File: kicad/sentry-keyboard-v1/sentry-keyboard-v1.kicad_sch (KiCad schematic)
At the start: 184 parts, among them J1 USB_C_Receptacle_USB2.0, J4 AVR-ISP-6, SW1 Reset, U1 ATmega32U4-AU, U3 PRTR5V0U2X, Y1 16Mhz

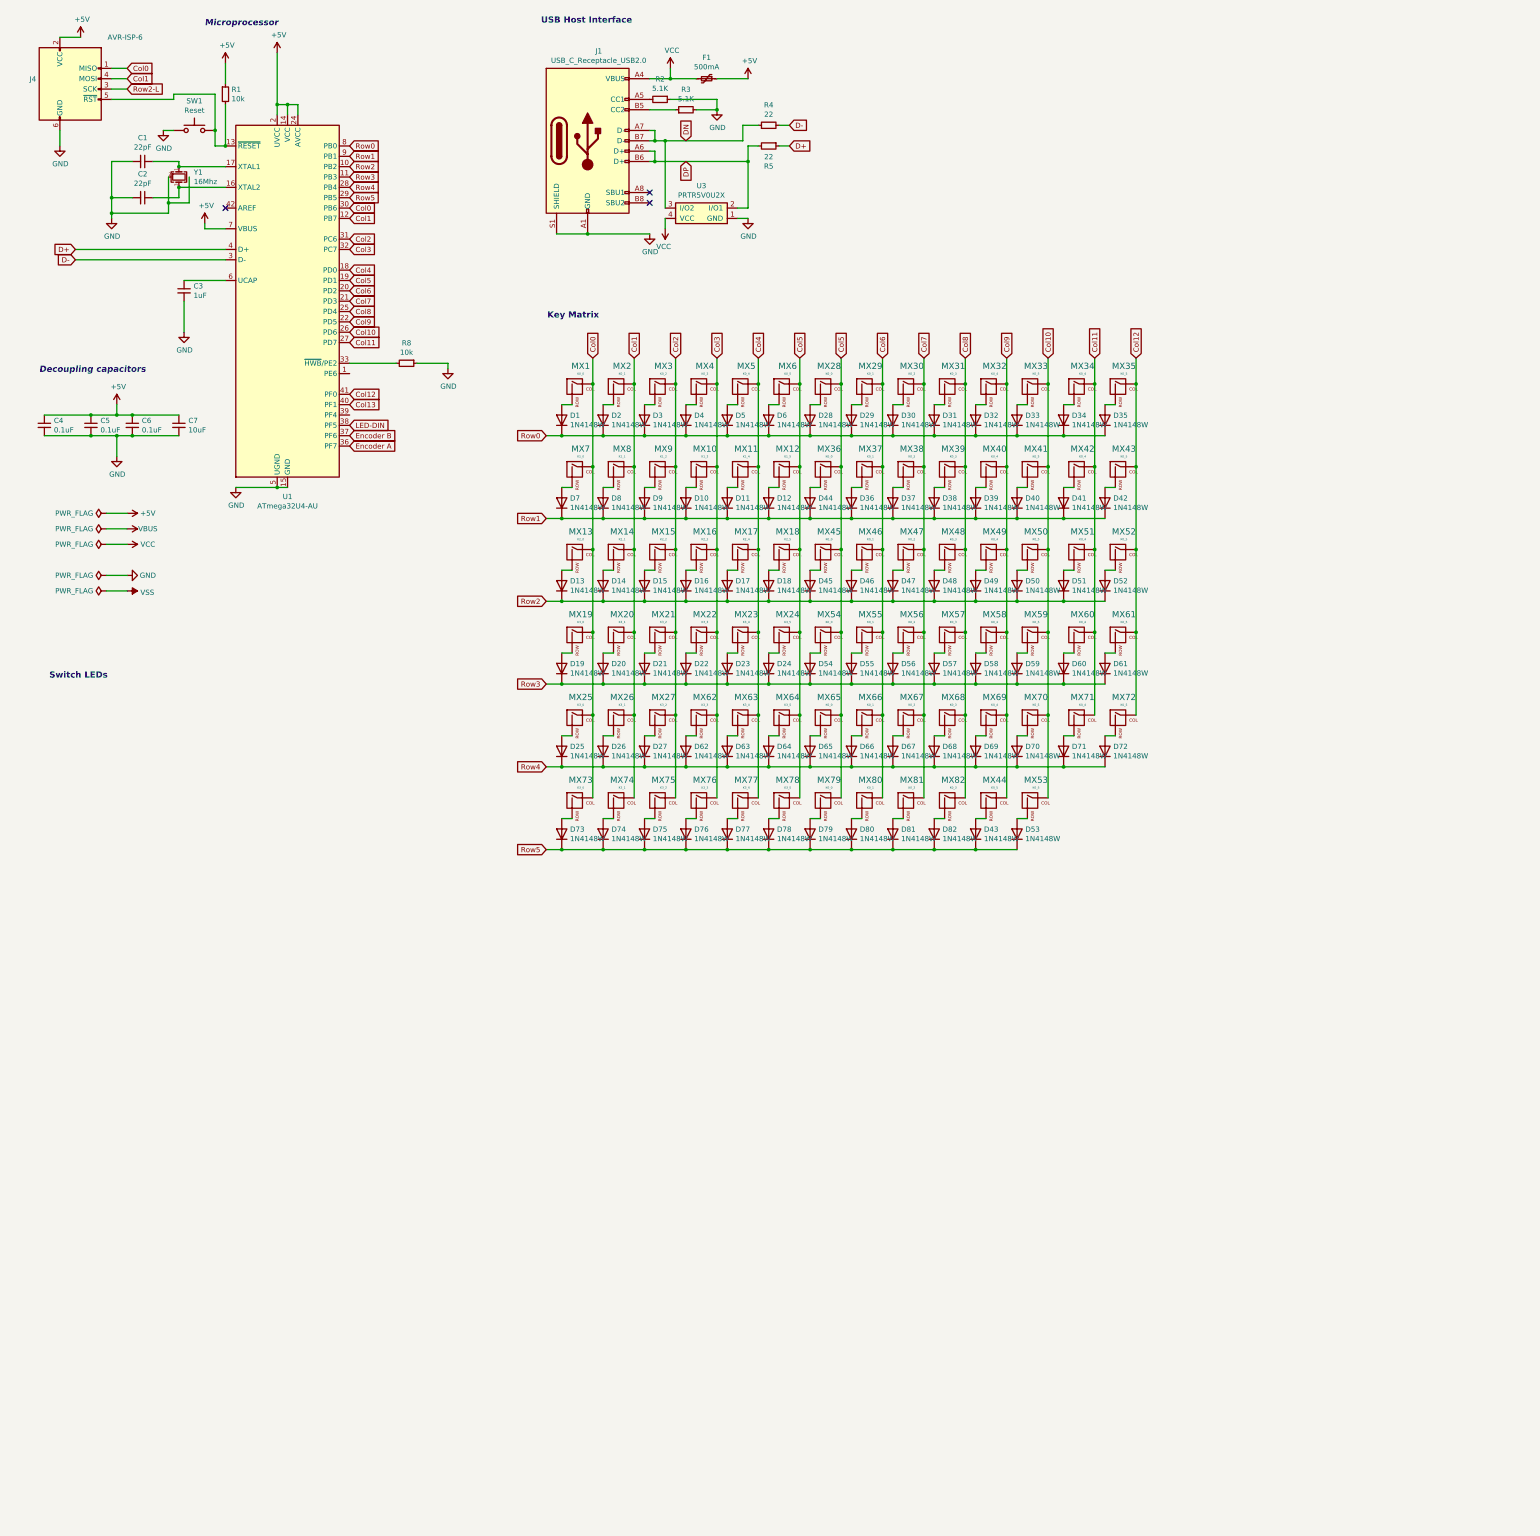
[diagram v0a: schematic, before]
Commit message: Add first draft of LED matrix
Need to figure out if each LED needs a 100uf capacitor, and if the data
line needs a resistor still. The datasheet is really hard to read
because of low quality scan.
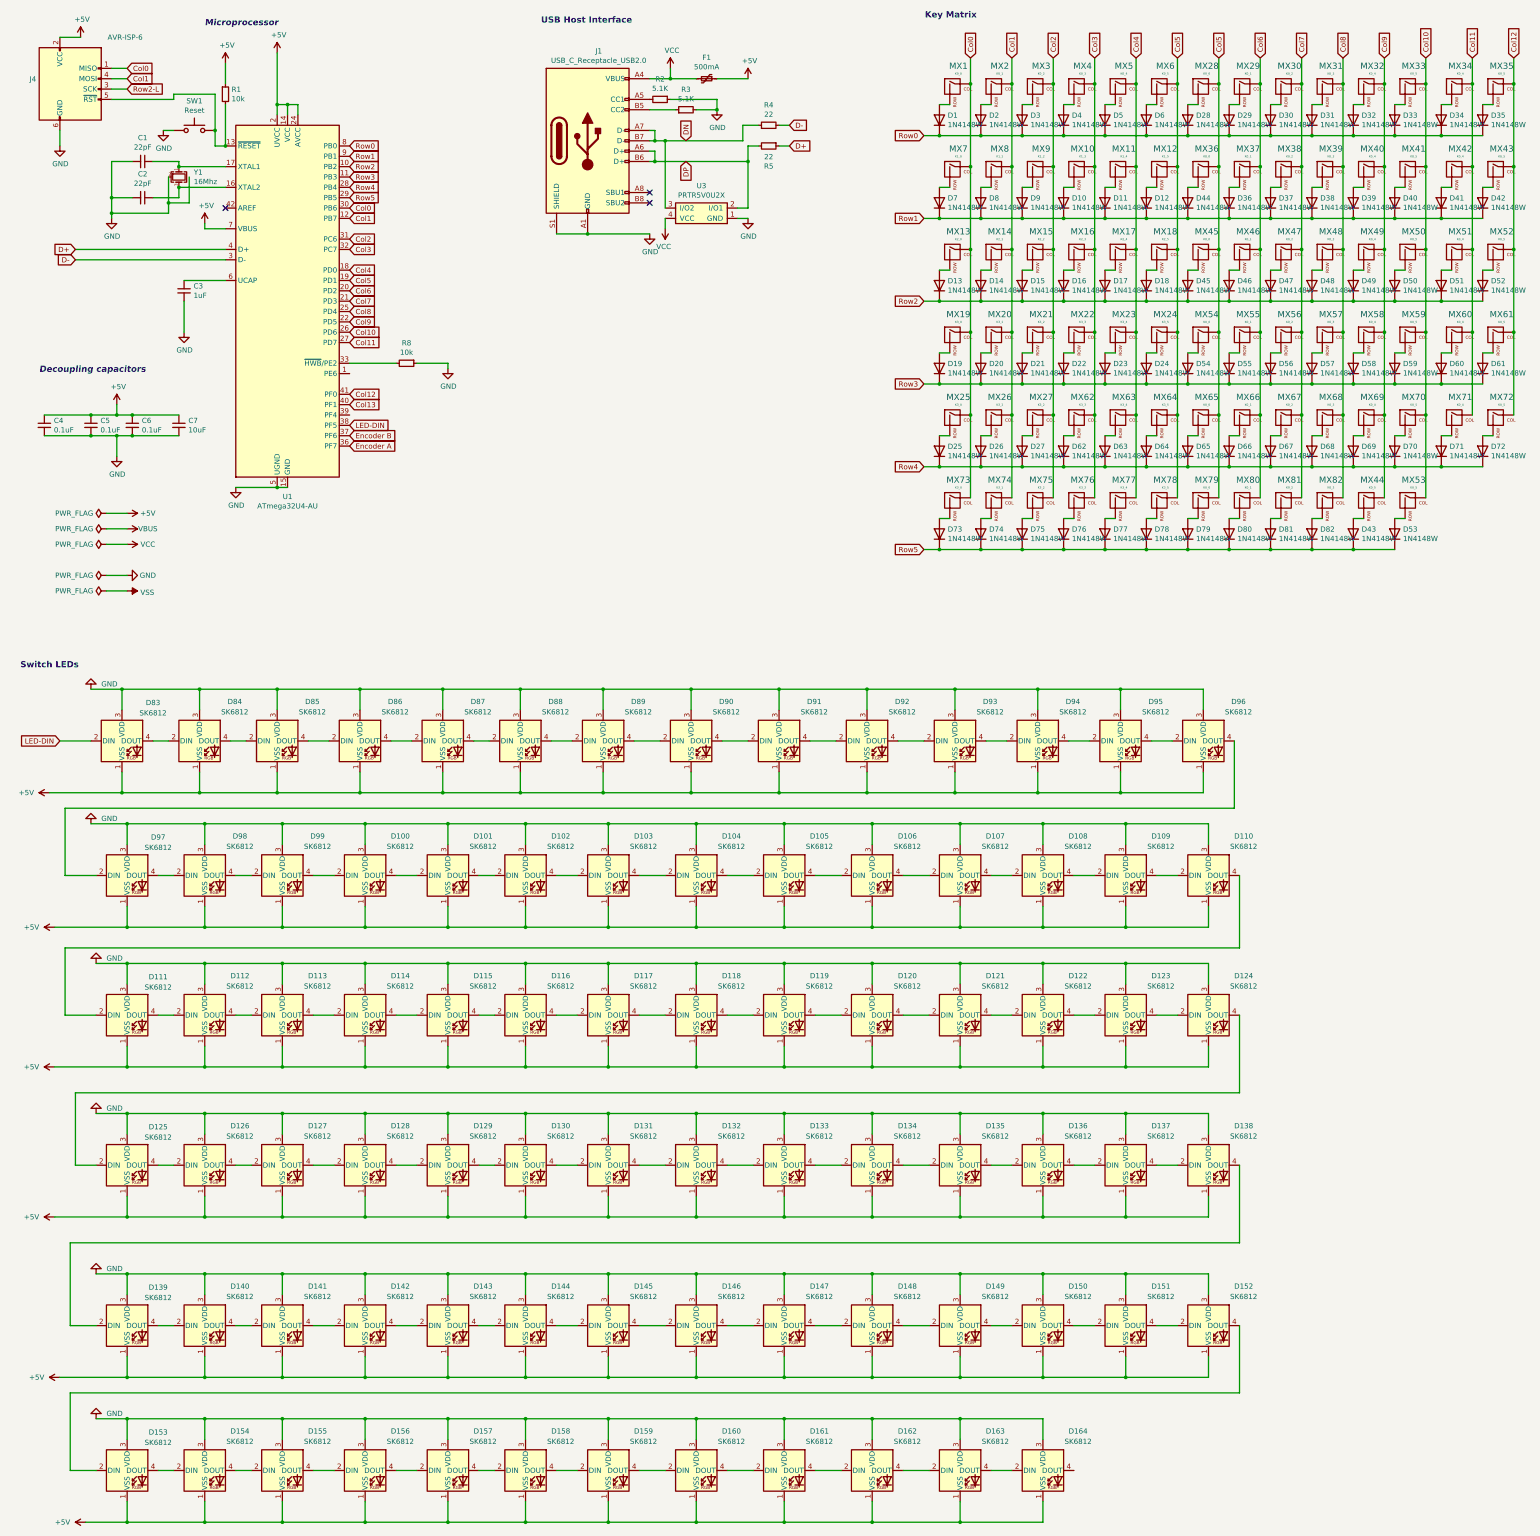
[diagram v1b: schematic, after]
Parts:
- added D100, D101, D102, D103, D104, D105, D106, D107, D108, D109, D110, D111, D112, D113, D114, D115, D116, D117, D118, D119, D120, D121, D122, D123, D124, D125, D126, D127, D128, D129, D130, D131, D132, D133, D134, D135, D136, D137, D138, D139, D140, D141, D142, D143, D144, D145, D146, D147, D148, D149, D150, D151, D152, D153, D154, D155, D156, D157, D158, D159, D160, D161, D162, D163, D164, D83, D84, D85, D86, D87, D88, D89, D90, D91, D92, D93, D94, D95, D96, D97, D98, D99: SK6812, LED_SMD:LED_SK6812_PLCC4_5.0x5.0mm_P3.2mm, symbol LED:SK6812
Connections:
- net +5V: now also D100.1 (VSS), D101.1 (VSS), D102.1 (VSS), D103.1 (VSS), D104.1 (VSS), D105.1 (VSS), D106.1 (VSS), D107.1 (VSS), D108.1 (VSS), D109.1 (VSS), D110.1 (VSS), D111.1 (VSS), D112.1 (VSS), D113.1 (VSS), D114.1 (VSS), D115.1 (VSS), D116.1 (VSS), D117.1 (VSS), D118.1 (VSS), D119.1 (VSS), D120.1 (VSS), D121.1 (VSS), D122.1 (VSS), D123.1 (VSS), D124.1 (VSS), D125.1 (VSS), D126.1 (VSS), D127.1 (VSS), D128.1 (VSS), D129.1 (VSS), D130.1 (VSS), D131.1 (VSS), D132.1 (VSS), D133.1 (VSS), D134.1 (VSS), D135.1 (VSS), D136.1 (VSS), D137.1 (VSS), D138.1 (VSS), D139.1 (VSS), D140.1 (VSS), D141.1 (VSS), D142.1 (VSS), D143.1 (VSS), D144.1 (VSS), D145.1 (VSS), D146.1 (VSS), D147.1 (VSS), D148.1 (VSS), D149.1 (VSS), D150.1 (VSS), D151.1 (VSS), D152.1 (VSS), D153.1 (VSS), D154.1 (VSS), D155.1 (VSS), D156.1 (VSS), D157.1 (VSS), D158.1 (VSS), D159.1 (VSS), D160.1 (VSS), D161.1 (VSS), D162.1 (VSS), D163.1 (VSS), D164.1 (VSS), D83.1 (VSS), D84.1 (VSS), D85.1 (VSS), D86.1 (VSS), D87.1 (VSS), D88.1 (VSS), D89.1 (VSS), D90.1 (VSS), D91.1 (VSS), D92.1 (VSS), D93.1 (VSS), D94.1 (VSS), D95.1 (VSS), D96.1 (VSS), D97.1 (VSS), D98.1 (VSS), D99.1 (VSS)
- net GND: now also D100.3 (VDD), D101.3 (VDD), D102.3 (VDD), D103.3 (VDD), D104.3 (VDD), D105.3 (VDD), D106.3 (VDD), D107.3 (VDD), D108.3 (VDD), D109.3 (VDD), D110.3 (VDD), D111.3 (VDD), D112.3 (VDD), D113.3 (VDD), D114.3 (VDD), D115.3 (VDD), D116.3 (VDD), D117.3 (VDD), D118.3 (VDD), D119.3 (VDD), D120.3 (VDD), D121.3 (VDD), D122.3 (VDD), D123.3 (VDD), D124.3 (VDD), D125.3 (VDD), D126.3 (VDD), D127.3 (VDD), D128.3 (VDD), D129.3 (VDD), D130.3 (VDD), D131.3 (VDD), D132.3 (VDD), D133.3 (VDD), D134.3 (VDD), D135.3 (VDD), D136.3 (VDD), D137.3 (VDD), D138.3 (VDD), D139.3 (VDD), D140.3 (VDD), D141.3 (VDD), D142.3 (VDD), D143.3 (VDD), D144.3 (VDD), D145.3 (VDD), D146.3 (VDD), D147.3 (VDD), D148.3 (VDD), D149.3 (VDD), D150.3 (VDD), D151.3 (VDD), D152.3 (VDD), D153.3 (VDD), D154.3 (VDD), D155.3 (VDD), D156.3 (VDD), D157.3 (VDD), D158.3 (VDD), D159.3 (VDD), D160.3 (VDD), D161.3 (VDD), D162.3 (VDD), D163.3 (VDD), D164.3 (VDD), D83.3 (VDD), D84.3 (VDD), D85.3 (VDD), D86.3 (VDD), D87.3 (VDD), D88.3 (VDD), D89.3 (VDD), D90.3 (VDD), D91.3 (VDD), D92.3 (VDD), D93.3 (VDD), D94.3 (VDD), D95.3 (VDD), D96.3 (VDD), D97.3 (VDD), D98.3 (VDD), D99.3 (VDD)
- net LED-DIN: now also D83.2 (DIN)
- new net: D83.4 (DOUT), D84.2 (DIN)
- new net: D84.4 (DOUT), D85.2 (DIN)
- new net: D100.2 (DIN), D99.4 (DOUT)
- new net: D100.4 (DOUT), D101.2 (DIN)
- new net: D119.4 (DOUT), D120.2 (DIN)
- new net: D120.4 (DOUT), D121.2 (DIN)
- new net: D137.4 (DOUT), D138.2 (DIN)
- new net: D138.4 (DOUT), D139.2 (DIN)
- new net: D149.4 (DOUT), D150.2 (DIN)
- new net: D150.4 (DOUT), D151.2 (DIN)
- new net: D132.4 (DOUT), D133.2 (DIN)
- new net: D133.4 (DOUT), D134.2 (DIN)
- new net: D126.4 (DOUT), D127.2 (DIN)
- new net: D127.4 (DOUT), D128.2 (DIN)
- new net: D90.4 (DOUT), D91.2 (DIN)
- new net: D91.4 (DOUT), D92.2 (DIN)
- new net: D106.4 (DOUT), D107.2 (DIN)
- new net: D107.4 (DOUT), D108.2 (DIN)
- new net: D151.4 (DOUT), D152.2 (DIN)
- new net: D92.4 (DOUT), D93.2 (DIN)
- new net: D93.4 (DOUT), D94.2 (DIN)
- new net: D135.4 (DOUT), D136.2 (DIN)
- new net: D136.4 (DOUT), D137.2 (DIN)
- new net: D111.4 (DOUT), D112.2 (DIN)
- new net: D112.4 (DOUT), D113.2 (DIN)
- new net: D134.4 (DOUT), D135.2 (DIN)
- new net: D147.4 (DOUT), D148.2 (DIN)
- new net: D148.4 (DOUT), D149.2 (DIN)
- new net: D128.4 (DOUT), D129.2 (DIN)
- new net: D129.4 (DOUT), D130.2 (DIN)
- new net: D113.4 (DOUT), D114.2 (DIN)
- new net: D152.4 (DOUT), D153.2 (DIN)
- new net: D156.4 (DOUT), D157.2 (DIN)
- new net: D157.4 (DOUT), D158.2 (DIN)
- new net: D163.4 (DOUT), D164.2 (DIN)
- new net: D142.4 (DOUT), D143.2 (DIN)
- new net: D143.4 (DOUT), D144.2 (DIN)
- new net: D124.4 (DOUT), D125.2 (DIN)
- new net: D125.4 (DOUT), D126.2 (DIN)
- new net: D161.4 (DOUT), D162.2 (DIN)
- new net: D162.4 (DOUT), D163.2 (DIN)
- new net: D139.4 (DOUT), D140.2 (DIN)
- new net: D140.4 (DOUT), D141.2 (DIN)
- new net: D144.4 (DOUT), D145.2 (DIN)
- new net: D130.4 (DOUT), D131.2 (DIN)
- new net: D131.4 (DOUT), D132.2 (DIN)
- new net: D158.4 (DOUT), D159.2 (DIN)
- new net: D159.4 (DOUT), D160.2 (DIN)
- new net: D109.4 (DOUT), D110.2 (DIN)
- new net: D110.4 (DOUT), D111.2 (DIN)
- new net: D97.4 (DOUT), D98.2 (DIN)
- new net: D98.4 (DOUT), D99.2 (DIN)
- new net: D104.4 (DOUT), D105.2 (DIN)
- new net: D105.4 (DOUT), D106.2 (DIN)
- new net: D145.4 (DOUT), D146.2 (DIN)
- new net: D146.4 (DOUT), D147.2 (DIN)
- new net: D108.4 (DOUT), D109.2 (DIN)
- new net: D121.4 (DOUT), D122.2 (DIN)
- new net: D122.4 (DOUT), D123.2 (DIN)
- new net: D154.4 (DOUT), D155.2 (DIN)
- new net: D155.4 (DOUT), D156.2 (DIN)
- new net: D86.4 (DOUT), D87.2 (DIN)
- new net: D87.4 (DOUT), D88.2 (DIN)
- new net: D123.4 (DOUT), D124.2 (DIN)
- new net: D114.4 (DOUT), D115.2 (DIN)
- new net: D85.4 (DOUT), D86.2 (DIN)
- new net: D88.4 (DOUT), D89.2 (DIN)
- new net: D96.4 (DOUT), D97.2 (DIN)
- new net: D95.4 (DOUT), D96.2 (DIN)
- new net: D89.4 (DOUT), D90.2 (DIN)
- new net: D94.4 (DOUT), D95.2 (DIN)
- new net: D141.4 (DOUT), D142.2 (DIN)
- new net: D103.4 (DOUT), D104.2 (DIN)
- new net: D153.4 (DOUT), D154.2 (DIN)
- new net: D160.4 (DOUT), D161.2 (DIN)
- new net: D115.4 (DOUT), D116.2 (DIN)
- new net: D101.4 (DOUT), D102.2 (DIN)
- new net: D116.4 (DOUT), D117.2 (DIN)
- new net: D102.4 (DOUT), D103.2 (DIN)
- new net: D117.4 (DOUT), D118.2 (DIN)
- new net: D118.4 (DOUT), D119.2 (DIN)
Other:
- moved on the sheet: D1, D10, D11, D12, D13, D14, D15, D16, D17, D18, D19, D2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

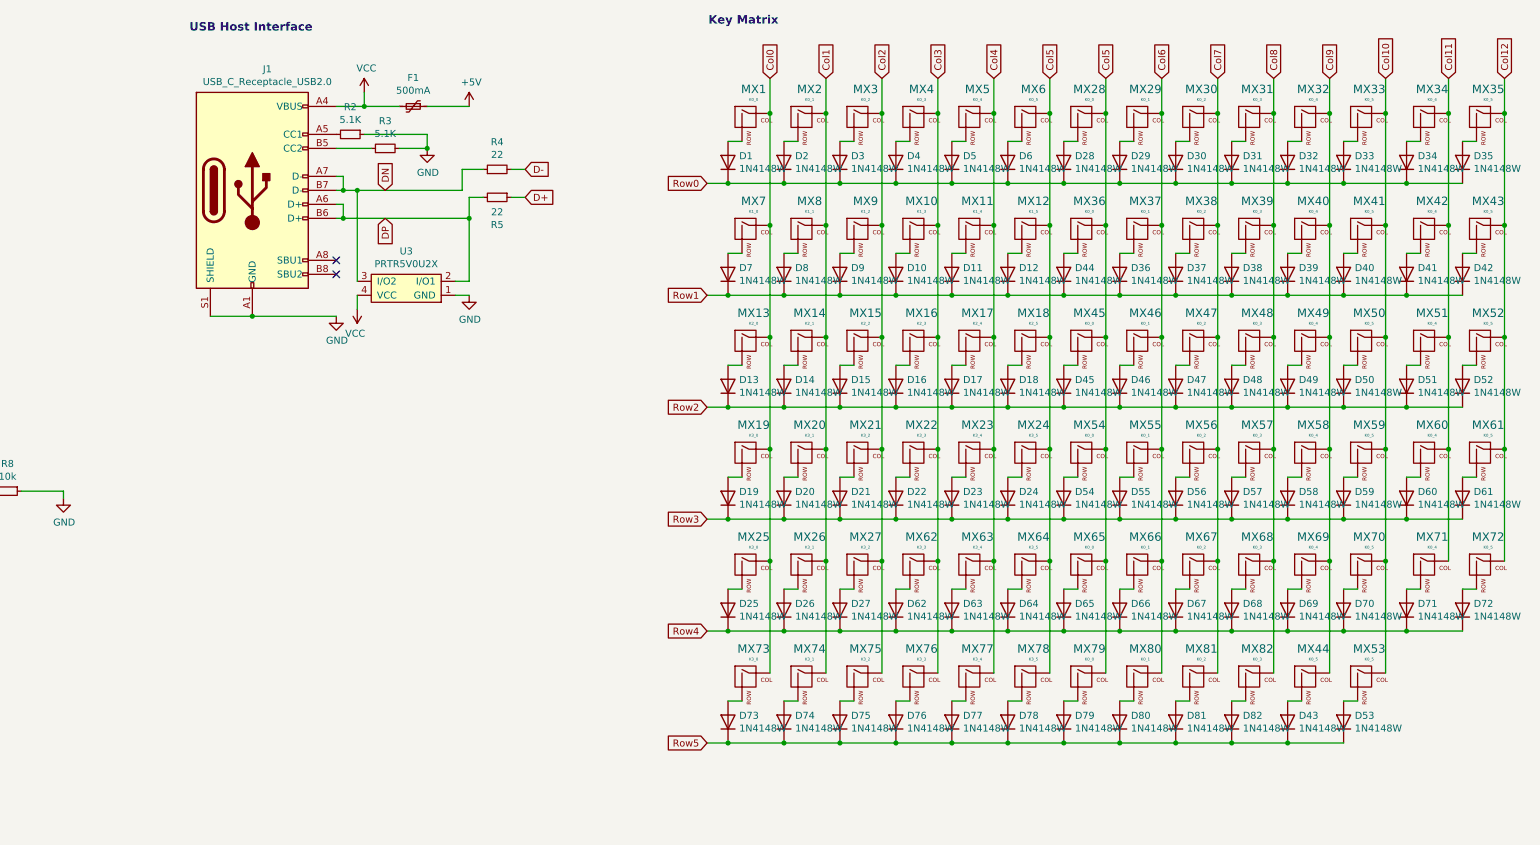
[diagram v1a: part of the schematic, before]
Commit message: Update schematic
- Label all the keys to make sure I have them all
- Reroute a few keys so that routing will be easier
- Wire up the switch on the encoder
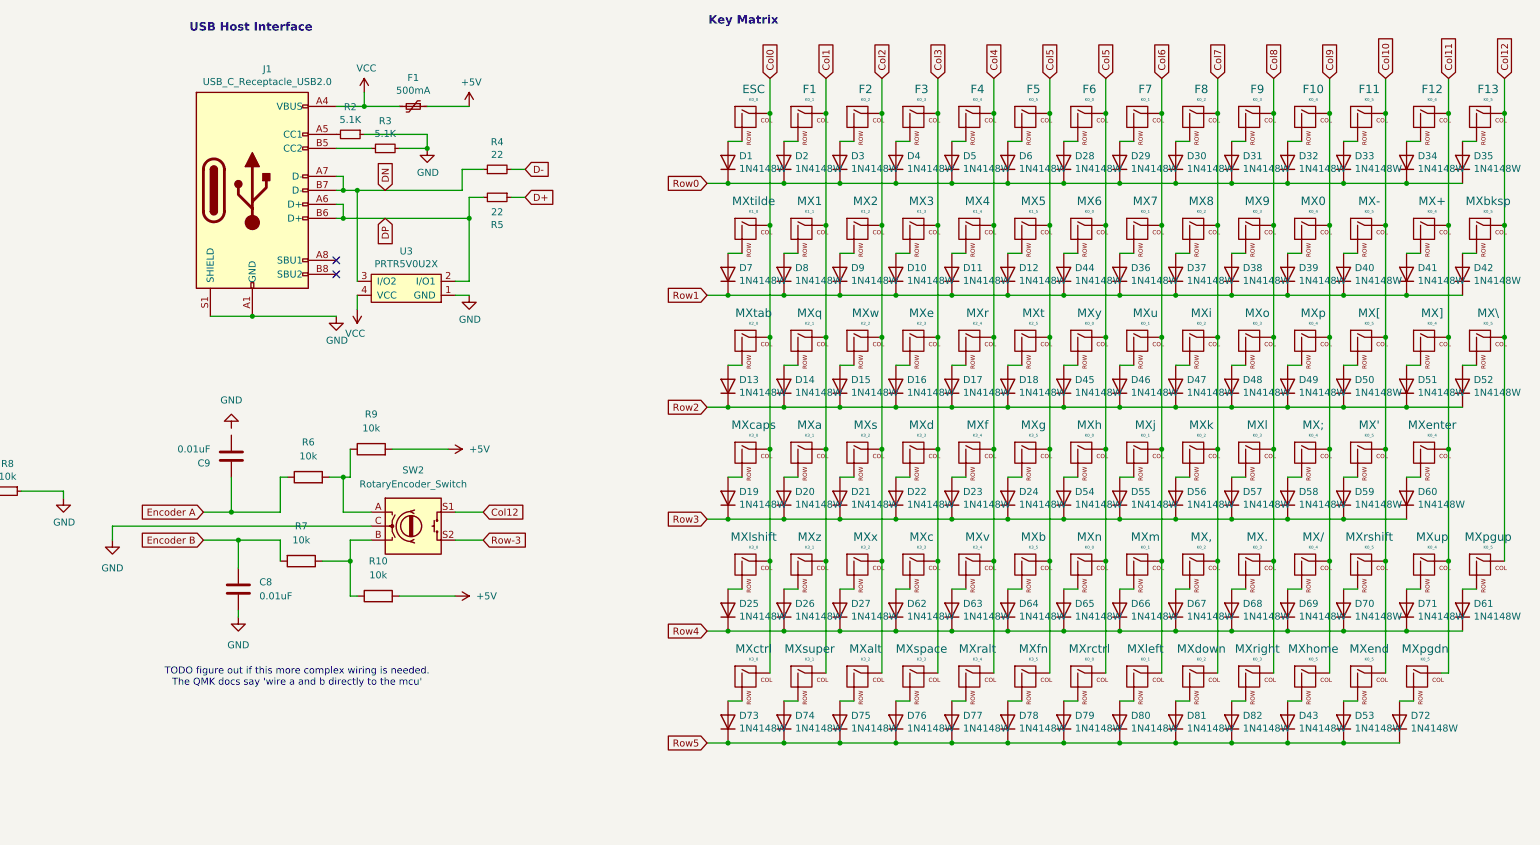
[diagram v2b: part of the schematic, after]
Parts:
- added C8, C9: 0.01uF, symbol Device:C
- added R10, R6, R7, R9: 10k, symbol Device:R
- added SW2: RotaryEncoder_Switch, symbol Device:RotaryEncoder_Switch
- J1: footprint Connector_USB:USB_C_Receptacle_HRO_TYPE-C-31-M-12 -> Connector_JST:JST_GH_SM05B-GHS-TB_1x05-1MP_P1.25mm_Horizontal
- renumbered MX1 to ESC, MX2 to F1, MX32 to F10, MX33 to F11, MX34 to F12, MX35 to F13, MX3 to F2, MX4 to F3, MX5 to F4, MX6 to F5, MX28 to F6, MX29 to F7, MX30 to F8, MX31 to F9, MX59 to MX', MX42 to MX+, MX67 to MX,, MX41 to MX-, MX68 to MX., MX69 to MX/, MX40 to MX0, MX8 to MX1, MX9 to MX2, MX10 to MX3, MX11 to MX4, MX12 to MX5, MX36 to MX6, MX37 to MX7, MX38 to MX8, MX39 to MX9, MX58 to MX;, MX50 to MX[, MX52 to MX\, MX51 to MX], MX20 to MXa, MX75 to MXalt, MX64 to MXb, MX43 to MXbksp, MX62 to MXc, MX19 to MXcaps, MX73 to MXctrl, MX22 to MXd, MX81 to MXdown, MX16 to MXe, MX53 to MXend, MX60 to MXenter, MX23 to MXf, MX78 to MXfn, MX24 to MXg, MX54 to MXh, MX44 to MXhome, MX47 to MXi, MX55 to MXj, MX56 to MXk, MX57 to MXl, MX80 to MXleft, MX25 to MXlshift, MX66 to MXm, MX65 to MXn, MX48 to MXo, MX49 to MXp, MX72 to MXpgdn, MX61 to MXpgup, MX14 to MXq, MX17 to MXr, MX77 to MXralt, MX79 to MXrctrl, MX82 to MXright, MX70 to MXrshift, MX21 to MXs, MX76 to MXspace, MX74 to MXsuper, MX18 to MXt, MX13 to MXtab, MX7 to MXtilde, MX46 to MXu, MX71 to MXup, MX63 to MXv, MX15 to MXw, MX27 to MXx, MX45 to MXy, MX26 to MXz
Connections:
- net +5V: now also R10.2, R9.2
- net Col11: now also MXpgdn.1 (COL)
- net Col12: now also SW2.S1; no longer MXpgdn.1 (COL)
- net Encoder A: now also C9.1, R6.1
- net Encoder B: now also C8.1, R7.2
- net GND: now also C8.2, SW2.C
- net Row3: no longer D61.1 (K)
- net Row4: now also D61.1 (K); no longer D72.1 (K)
- net Row5: now also D72.1 (K)
- new net: R10.1, R7.1, SW2.B
- new net: R6.2, R9.1, SW2.A
- new net Row-3: SW2.S2
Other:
- note added: "TODO figure out if this more complex wiring is needed. The QMK docs say 'wire a and b directly to the mcu'"
- moved on the sheet: D61, D72, MXpgdn, MXpgup
